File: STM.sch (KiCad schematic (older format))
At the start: 17 parts, among them J3 Micro_SD_Card_Det, J4 TagConnect_TC2030_SWD, Q9 AO3401A, SW8 POWER, U8 STM32L151C8Tx

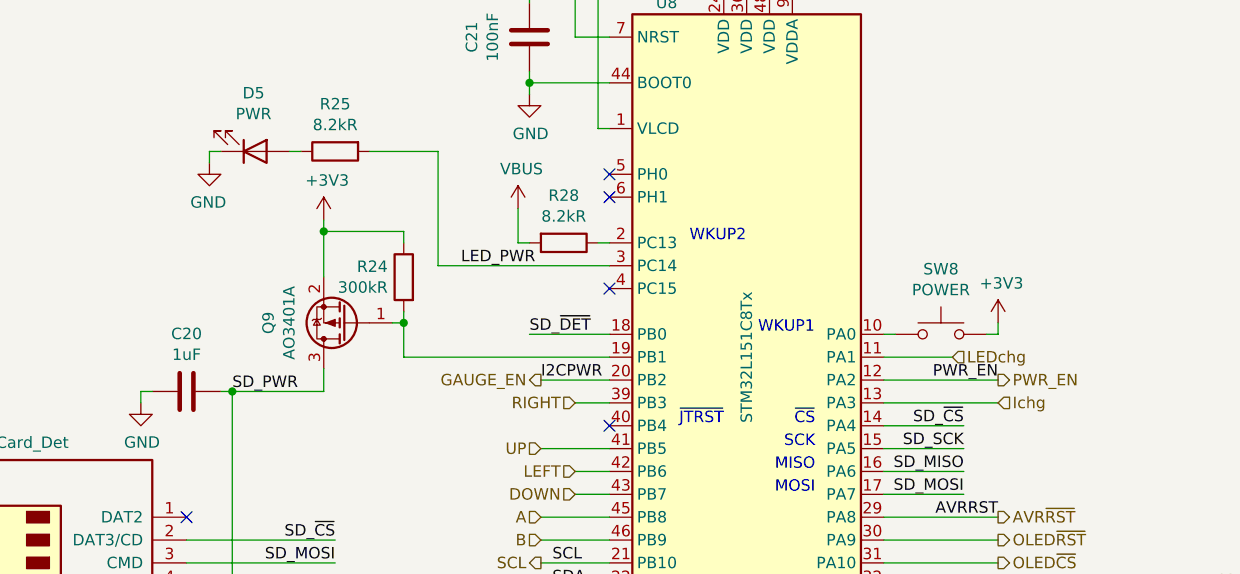
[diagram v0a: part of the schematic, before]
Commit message: Place and route WS2812 LEDs
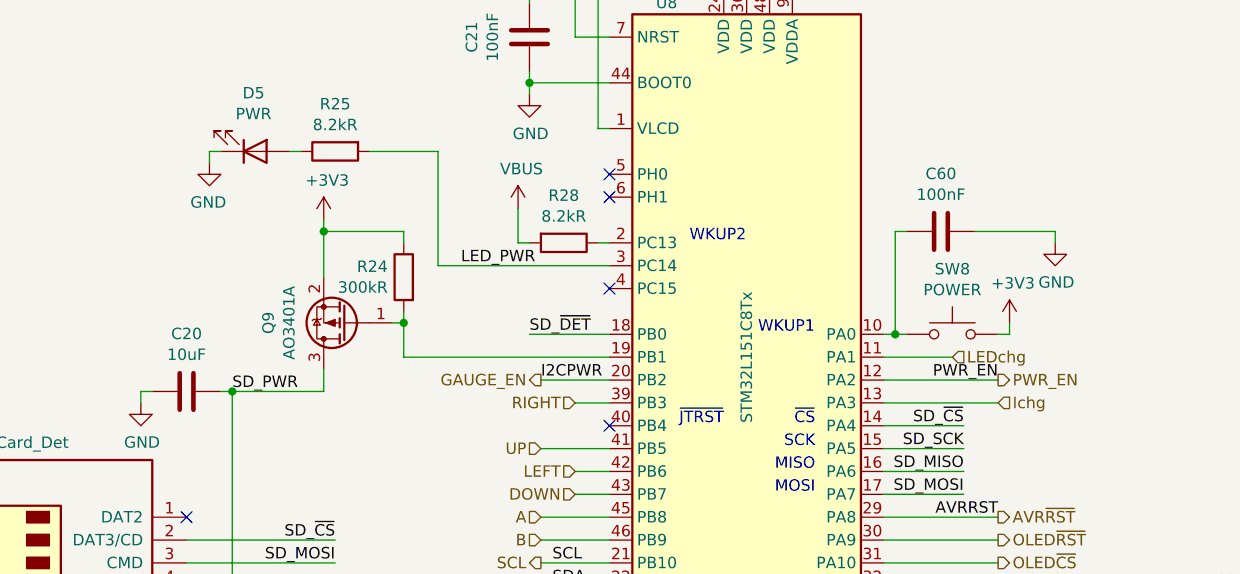
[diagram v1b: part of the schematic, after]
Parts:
- added C60: 100nF, Capacitor_SMD:C_0402_1005Metric, symbol Device:C
- C20: value 1uF -> 10uF; footprint Capacitor_SMD:C_0402_1005Metric -> Capacitor_SMD:C_0603_1608Metric; LCSC C52923 -> C19702
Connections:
- net GND: now also C20.1, C60.2; no longer C20.2
- net SD_PWR: now also C20.2; no longer C20.1
- net at SW8.1, U8.10 (PA0): now also C60.1
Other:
- moved on the sheet: SW8
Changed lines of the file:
@@
 $Descr A4 11693 8268
 encoding utf-8
-Sheet 4 23
+Sheet 4 17
 Title ""
 Date ""
@@
 L Switch:SW_Push SW?
 U 1 1 60D10149
-P 6900 3800
+P 6950 3800
 AR Path="/60D10149" Ref="SW?"  Part="1"
 AR Path="/6051E9DC/60D10149" Ref="SW?"  Part="1"
 AR Path="/60CF39C0/60D10149" Ref="SW8"  Part="1"
-F 0 "SW8" H 6900 4085 50  0000 C CNN
-F 1 "POWER" H 6900 3994 50  0000 C CNN
-F 2 "Button_Carbon:Button_Carbon_5mm" H 6900 4000 50  0001 C CNN
-F 3 "~" H 6900 4000 50  0001 C CNN
-	1    6900 3800
-	1    0    0    -1
-$EndComp
-Wire Wire Line
-	7150 3800 7100 3800
+F 0 "SW8" H 6950 4085 50  0000 C CNN
+F 1 "POWER" H 6950 3994 50  0000 C CNN
+F 2 "Button_Carbon:Button_Carbon_5mm" H 6950 4000 50  0001 C CNN
+F 3 "~" H 6950 4000 50  0001 C CNN
+	1    6950 3800
+	1    0    0    -1
+$EndComp
+Wire Wire Line
+	7200 3800 7150 3800
 $Comp
 L power:+3V3 #PWR?
 U 1 1 60D10150
-P 7150 3750
+P 7200 3750
 AR Path="/6051E9DC/60D10150" Ref="#PWR?"  Part="1"
 AR Path="/60CF39C0/60D10150" Ref="#PWR0106"  Part="1"
-F 0 "#PWR0106" H 7150 3600 50  0001 C CNN
-F 1 "+3V3" H 7165 3923 50  0000 C CNN
-F 2 "" H 7150 3750 50  0001 C CNN
-F 3 "" H 7150 3750 50  0001 C CNN
-	1    7150 3750
-	1    0    0    -1
-$EndComp
-Wire Wire Line
-	7150 3750 7150 3800
+F 0 "#PWR0106" H 7200 3600 50  0001 C CNN
+F 1 "+3V3" H 7215 3923 50  0000 C CNN
+F 2 "" H 7200 3750 50  0001 C CNN
+F 3 "" H 7200 3750 50  0001 C CNN
+	1    7200 3750
+	1    0    0    -1
+$EndComp
+Wire Wire Line
+	7200 3750 7200 3800
 $Comp
 L Connector_TagConnect:TagConnect_TC2030_SWD J?
@@
 	6650 1950 6650 1550
 Wire Wire Line
-	6700 3800 6650 3800
-Wire Wire Line
 	5450 2900 5400 2900
 Wire Wire Line
@@
 	3800 5100 3600 5100
 Connection ~ 3800 5500
-$Comp
-L Device:C C?
-U 1 1 60D10227
-P 3600 4050
-AR Path="/60D10227" Ref="C?"  Part="1"
-AR Path="/634EFCCB/60D10227" Ref="C?"  Part="1"
-AR Path="/60049FDA/60D10227" Ref="C?"  Part="1"
-AR Path="/6051E9DC/60D10227" Ref="C?"  Part="1"
-AR Path="/60CF39C0/60D10227" Ref="C20"  Part="1"
-F 0 "C20" V 3348 4050 50  0000 C CNN
-F 1 "1uF" V 3439 4050 50  0000 C CNN
-F 2 "Capacitor_SMD:C_0402_1005Metric" H 3638 3900 50  0001 C CNN
-F 3 "~" H 3600 4050 50  0001 C CNN
-F 4 "C52923" V 3600 4050 50  0001 C CNN "LCSC"
-	1    3600 4050
-	0    1    1    0
-$EndComp
 Wire Wire Line
 	3600 4900 3800 4900
@@
 Text HLabel 5300 4500 0    50   Input ~ 0
 DOWN
+$Comp
+L Device:C C?
+U 1 1 6235648D
+P 6900 3350
+AR Path="/6235648D" Ref="C?"  Part="1"
+AR Path="/6051E9DC/6235648D" Ref="C?"  Part="1"
+AR Path="/60CF39C0/6235648D" Ref="C60"  Part="1"
+F 0 "C60" V 7152 3350 50  0000 C CNN
+F 1 "100nF" V 7061 3350 50  0000 C CNN
+F 2 "Capacitor_SMD:C_0402_1005Metric" H 6938 3200 50  0001 C CNN
+F 3 "~" H 6900 3350 50  0001 C CNN
+F 4 "C1525" H 6900 3350 50  0001 C CNN "LCSC"
+	1    6900 3350
+	0    -1   -1   0
+$EndComp
+Wire Wire Line
+	6650 3800 6700 3800
+Wire Wire Line
+	6700 3800 6700 3350
+Wire Wire Line
+	6700 3350 6750 3350
+Connection ~ 6700 3800
+Wire Wire Line
+	6700 3800 6750 3800
+$Comp
+L power:GND #PWR0191
+U 1 1 62369F47
+P 7400 3400
+F 0 "#PWR0191" H 7400 3150 50  0001 C CNN
+F 1 "GND" H 7405 3227 50  0000 C CNN
+F 2 "" H 7400 3400 50  0001 C CNN
+F 3 "" H 7400 3400 50  0001 C CNN
+	1    7400 3400
+	1    0    0    -1
+$EndComp
+Wire Wire Line
+	7050 3350 7400 3350
+Wire Wire Line
+	7400 3350 7400 3400
+$Comp
+L Device:C C?
+U 1 1 6237296F
+P 3600 4050
+AR Path="/6051E9DC/6237296F" Ref="C?"  Part="1"
+AR Path="/60CF39C0/6237296F" Ref="C20"  Part="1"
+F 0 "C20" V 3852 4050 50  0000 C CNN
+F 1 "10uF" V 3761 4050 50  0000 C CNN
+F 2 "Capacitor_SMD:C_0603_1608Metric" H 3638 3900 50  0001 C CNN
+F 3 "~" H 3600 4050 50  0001 C CNN
+F 4 "C19702" V 3600 4050 50  0001 C CNN "LCSC"
+	1    3600 4050
+	0    -1   -1   0
+$EndComp
 $EndSCHEMATC

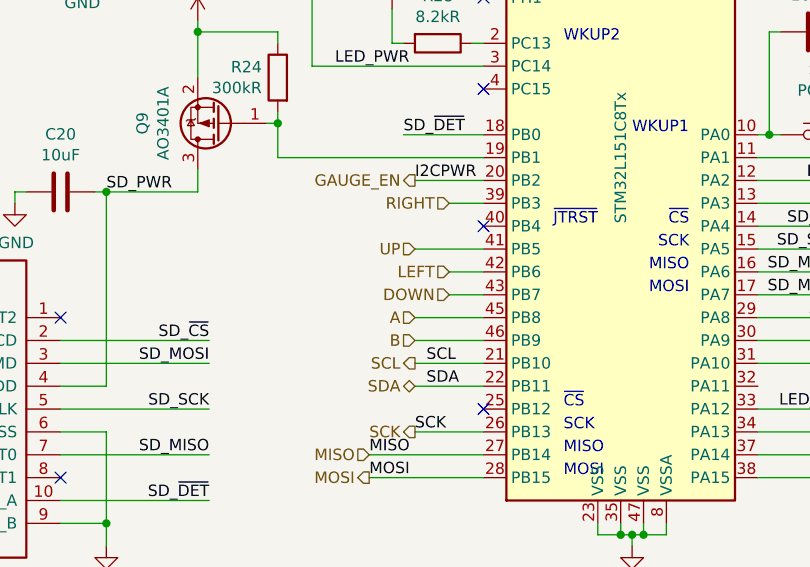
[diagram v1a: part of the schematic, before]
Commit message: Implement elevated AB surfaces
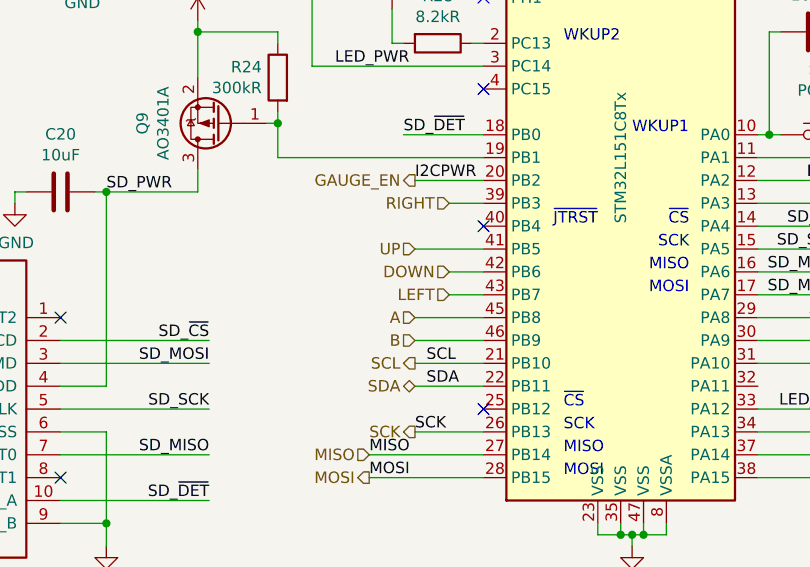
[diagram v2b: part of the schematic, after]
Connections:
- net DOWN: now also U8.42 (PB6); no longer U8.43 (PB7)
- net LEFT: now also U8.43 (PB7); no longer U8.42 (PB6)
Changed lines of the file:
@@
 Text HLabel 5150 4300 0    50   Input ~ 0
 UP
-Text HLabel 5300 4400 0    50   Input ~ 0
+Text HLabel 5300 4500 0    50   Input ~ 0
 LEFT
 Wire Wire Line
-	5300 4400 5450 4400
+	5300 4500 5450 4500
 Text HLabel 5300 4100 0    50   Input ~ 0
 RIGHT
@@
 Connection ~ 3800 4050
 Wire Wire Line
-	5300 4500 5450 4500
-Text HLabel 5300 4500 0    50   Input ~ 0
+	5300 4400 5450 4400
+Text HLabel 5300 4400 0    50   Input ~ 0
 DOWN
 $Comp

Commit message: Use tactile power switch
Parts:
- SW8: footprint Button_Carbon:Button_Carbon_5mm -> XKB_switch:TS-1187A-X-X-X; LCSC (none) -> C318886
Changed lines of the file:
@@
 F 0 "SW8" H 6950 4085 50  0000 C CNN
 F 1 "POWER" H 6950 3994 50  0000 C CNN
-F 2 "Button_Carbon:Button_Carbon_5mm" H 6950 4000 50  0001 C CNN
+F 2 "XKB_switch:TS-1187A-X-X-X" H 6950 4000 50  0001 C CNN
 F 3 "~" H 6950 4000 50  0001 C CNN
+F 4 "C318886" H 6950 3800 50  0001 C CNN "LCSC"
 	1    6950 3800
 	1    0    0    -1

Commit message: Fix LCSC partnumbers
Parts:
- U8: LCSC C9861 -> C95578
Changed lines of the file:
@@
 F 2 "Package_QFP:LQFP-48_7x7mm_P0.5mm" H 5550 2400 50  0001 R CNN
 F 3 "http://www.st.com/st-web-ui/static/active/en/resource/technical/document/datasheet/CD00277537.pdf" H 6050 3900 50  0001 C CNN
-F 4 "C9861" H 6050 3900 50  0001 C CNN "LCSC"
+F 4 "C95578" H 6050 3900 50  0001 C CNN "LCSC"
 	1    6050 3900
 	1    0    0    -1
